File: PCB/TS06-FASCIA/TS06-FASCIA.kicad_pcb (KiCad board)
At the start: 2 copper layers, 176 x 52 mm, 18 parts, among them J1 PH 6, SW1 SR25 6-pos, SW2 FIELD, SW3 SUB, SW4 MINUS, SW5 PLUS

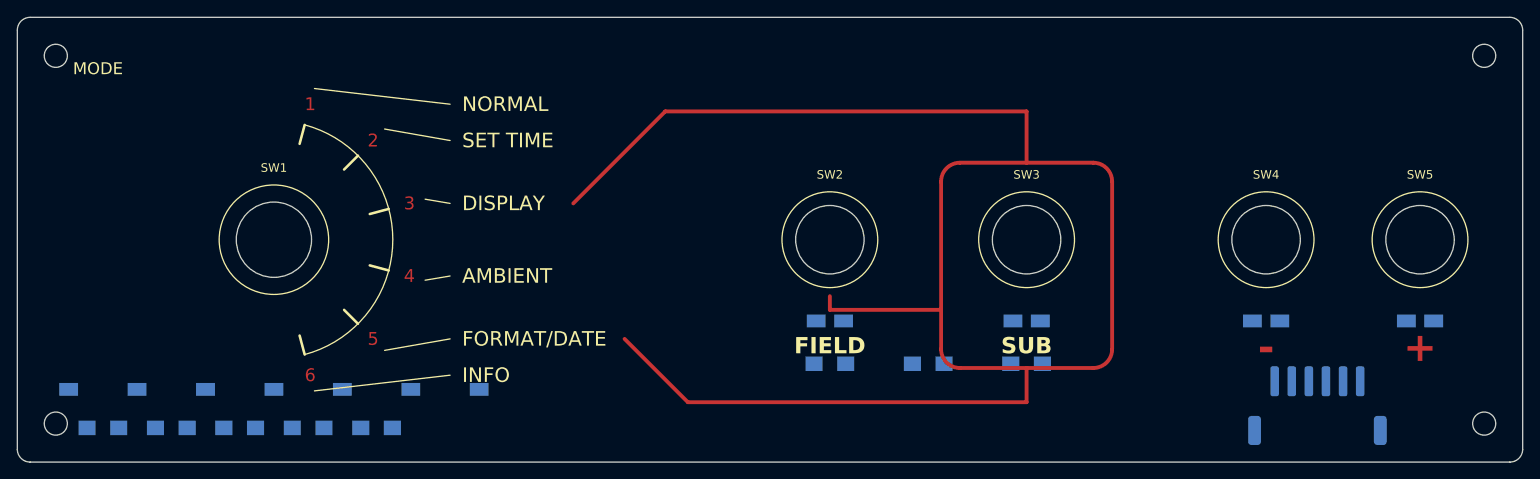
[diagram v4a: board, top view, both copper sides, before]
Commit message: Route TS06-FASCIA on two layers; link the schematic to the board
43 tracks, 7 vias, both clearance and connectivity checks clean at 0.2mm.

TWO LAYERS, deliberately. The front of this board is copper too, and a trace there is
invisible: solder mask is opaque, so only the deliberate mask openings show gold. That
makes F.Cu a free routing layer for anything clear of the decorative copper. All seven
vias are tented and sit at y > 45, in the band the chassis recess covers. Single-layer
was attempted first and does not fit: the switch body keepouts occupy everything above
y=38, leaving a 13mm band that already holds the landing pads, both resistor rows and
the connector - four buses through that means clearances under 0.5mm.

  B.Cu  the ladder, every local hop, the GND bus along the bottom edge, and A7
  F.Cu  the two long hauls, +5V at y=50 and A6 at y=47.2

J1's pin order is now chosen by the PCB rather than by tidiness - D8, D7, GND, A7,
+5V, A6 - so each net lands on the pin nearest the direction it arrives from and no
two traces cross to reach the connector. The schematic was regenerated to match.

Two crossings the checker caught and I fixed: both button grounds sat inside A7's lane
and could not drop straight to the bus, so they now collect above the button pads and
come down the right-hand edge. LEVB has the same problem and hops to the front for
2.3mm, landing inside the SUB box outline where the front is empty copper anyway.

New tool: tools/checkcopper.py - track/pad, track/track, via clearance per layer, plus
two things a naive checker misses. The decorative gold is NETLESS COPPER, so a routed
trace touching it is a short rather than an overlap; and gr_text on F.Cu is copper too,
so the dial numerals and the +/- glyphs get bounding boxes. Both are now checked.

Also fixed in tools/checksch.py: labels dropped on the MIDDLE of a wire were ignored,
which made correctly-named nets report as unnamed. KiCad attaches them; now so does the
checker.

The two files no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
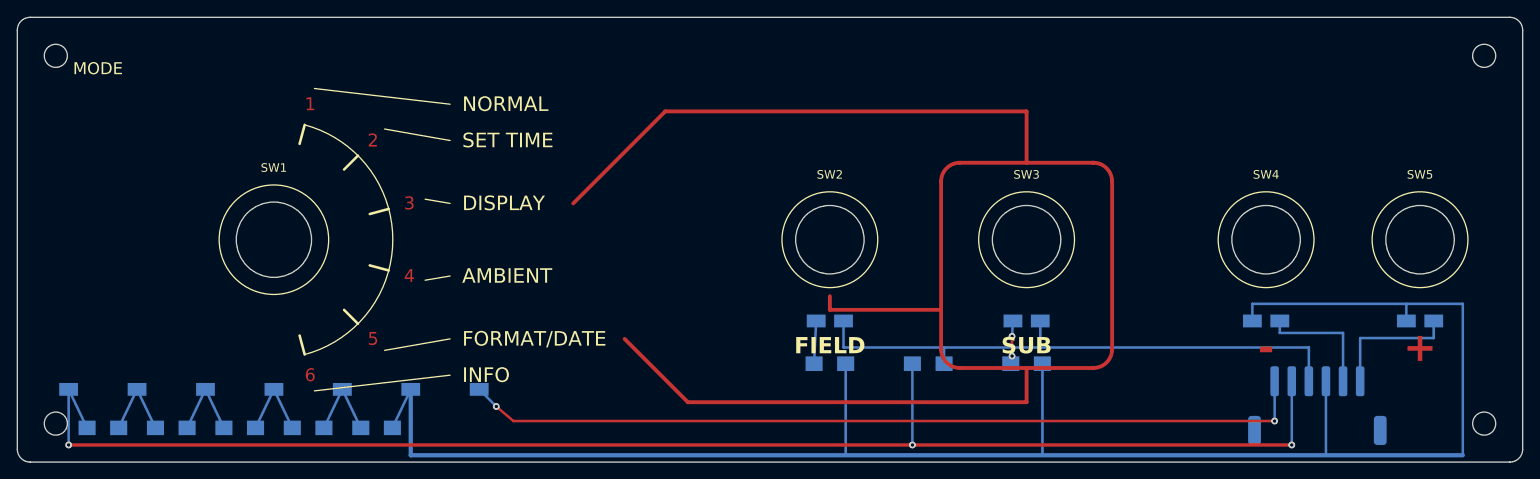
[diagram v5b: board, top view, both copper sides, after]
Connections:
- J1 pad 1: GND -> D8
- J1 pad 2: +5V -> D7
- J1 pad 3: A6 -> GND
- J1 pad 5: D7 -> +5V
- J1 pad 6: D8 -> A6
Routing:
- net GND: track 0.00 -> 212.0 mm
- net +5V: track 0.00 -> 171.4 mm, vias 0 -> 3
- net A6: track 0.00 -> 99.1 mm, vias 0 -> 2
- net A7: track 0.00 -> 66.5 mm
- net D8: track 0.00 -> 15.6 mm
- net D7: track 0.00 -> 14.5 mm
- net TAP5: track 0.00 -> 9.97 mm
- net TAP4: track 0.00 -> 9.97 mm
- net TAP3: track 0.00 -> 9.97 mm
- net TAP2: track 0.00 -> 9.97 mm
- net LEVB: track 0.00 -> 5.02 mm, vias 0 -> 2
- net LEVA: track 0.00 -> 5.01 mm
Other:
- board text added: "1 D8 2 D7 3 GND 4 A7 5 +5V 6 A6"
- board text removed: "1 GND 2 +5V 3 A6 4 A7 5 D7 6 D8"
